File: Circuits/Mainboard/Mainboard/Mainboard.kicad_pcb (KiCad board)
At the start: 2 copper layers, 170 x 170 mm, 96 parts, among them IC1 LM74500QDDFRQ1, IC2 LM74500QDDFRQ1, IC3 2536030320001, IC4 SX1280IMLTRT, IC5 SKY66122-11, IC6 TPS563300DRLR, IC7 TPS563300DRLR, J1 XT60PW-M, J10 B5P-VH_LF__SN_, J11 B6B-PH-K-S, J12 B5P-VH_LF__SN_, J13 B6B-PH-K-S, J14 B5P-VH_LF__SN_, J15 SMA-J-P-H-RA-TH1, J16 B5P-VH_LF__SN_, J17 Conn_01x04_Pin, J2 XT60PW-M, J23 Conn_01x04_Pin, J24 Conn_01x06_Pin, J25 Conn_01x06_Pin, J26 Conn_01x04_Pin, J27 Conn_01x04_Pin, J3 Conn_01x06_Pin, J5 B6B-PH-K-S, J6 B5P-VH_LF__SN_, J7 B6B-PH-K-S, J8 Conn_01x06_Pin, J9 Conn_01x04_Pin, P1 66200621122, Q1 PSMN6R7-40MLDX, Q2 PSMN6R7-40MLDX, U1 NUCLEOH723ZG, U2 ADP121-AUJZ28R7

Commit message: Routing tracks
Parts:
- removed C14: 0.1uF, Capacitor_SMD:C_0805_2012Metric_Pad1.18x1.45mm_HandSolder
- removed C15, C17, C29, C31, C33: 100nF, Capacitor_SMD:C_0805_2012Metric_Pad1.18x1.45mm_HandSolder
- removed C16, C18, C30, C32, C34: 1nF, Capacitor_SMD:C_0805_2012Metric_Pad1.18x1.45mm_HandSolder
- removed C19: 1uF, Capacitor_SMD:C_0805_2012Metric_Pad1.18x1.45mm_HandSolder
- removed C20, C21: 10nF, Capacitor_SMD:C_0805_2012Metric_Pad1.18x1.45mm_HandSolder
- removed C35: 0p8, Capacitor_SMD:C_0805_2012Metric_Pad1.18x1.45mm_HandSolder
- removed C36: 1p5, Capacitor_SMD:C_0805_2012Metric_Pad1.18x1.45mm_HandSolder
- removed C37, C42: NA, Capacitor_SMD:C_0805_2012Metric_Pad1.18x1.45mm_HandSolder
- removed C38: 0p5, Capacitor_SMD:C_0805_2012Metric_Pad1.18x1.45mm_HandSolder
- removed C39: 100p, Capacitor_SMD:C_0805_2012Metric_Pad1.18x1.45mm_HandSolder
- removed C40: 47p, Capacitor_SMD:C_0805_2012Metric_Pad1.18x1.45mm_HandSolder
- removed C41: 0p6, Capacitor_SMD:C_0805_2012Metric_Pad1.18x1.45mm_HandSolder
- removed FB1, FB2: 120R, Resistor_SMD:R_0805_2012Metric_Pad1.20x1.40mm_HandSolder
- removed IC4: SX1280IMLTRT, SX1280IMLTRT:QFN50P400X400X100-25N-D
- removed IC5: SKY66122-11, SKY66122-11:QFN50P400X400X100-25N-D
- removed J15: SMA-J-P-H-RA-TH1, SMA-J-P-H-RA-TH1:SMAJPHRATH1
- removed R5: 3n, Resistor_SMD:R_0805_2012Metric_Pad1.20x1.40mm_HandSolder
- removed R6: 2n7, Resistor_SMD:R_0805_2012Metric_Pad1.20x1.40mm_HandSolder
- removed R7: 3n9, Resistor_SMD:R_0805_2012Metric_Pad1.20x1.40mm_HandSolder
- moved C24 156.3 mm to (198.9, 122.0), turned to -90 degrees
- moved C23 143.0 mm to (196.5, 139.8), turned to 180 degrees
- moved P1 138.6 mm to (254.9, 161.4), turned to 90 degrees
- moved C25 135.4 mm to (201.8, 122.0), turned to -90 degrees
- moved C26 130.6 mm to (195.3, 123.5)
- moved L2 126.7 mm to (194.3, 131.7)
- moved C13 126.5 mm to (175.8, 132.5)
- moved C10 126.1 mm to (190.1, 147.6)
- moved C7 126.0 mm to (190.7, 150.4)
- moved C12 123.0 mm to (167.2, 120.1), turned to -90 degrees
- moved C22 115.6 mm to (190.5, 140.6), turned to 180 degrees
- moved IC6 114.8 mm to (190.3, 144.4), turned to 90 degrees
- moved IC3 107.2 mm to (194.7, 120.2)
- moved R9 107.1 mm to (198.1, 144.7), turned to 90 degrees
- moved C44 104.1 mm to (169.6, 129.6)
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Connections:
- P1 pad 4: unconnected-(P1-Pad4) -> /LT3751_GPIO_INPUT
- P1 pad 5: unconnected-(P1-Pad5) -> /LT3751_GPIO_OUTPUT
- U1 pad CN8_7: 3.3V -> unconnected-(U1C-3V3_CN8-PadCN8_7)
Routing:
- net /VL6180_IO0: track 0.00 -> 157.9 mm, vias 0 -> 3
- net /M3_Encoder_A: track 0.00 -> 130.8 mm, vias 0 -> 1
- net /VL6180_SCL: track 0.00 -> 129.4 mm, vias 0 -> 3
- net /VL53L4CD_SDA: track 0.00 -> 112.8 mm, vias 0 -> 7
- net /ADPS-9960_INT: track 0.00 -> 110.9 mm, vias 0 -> 5
- net /ADPS-9960_SCL: track 0.00 -> 110.9 mm, vias 0 -> 3
- net /ADPS-9960_VL: track 0.00 -> 110.7 mm, vias 0 -> 2
- net /Rpi_RX: track 0.00 -> 109.0 mm, vias 0 -> 2
- net /M1_RX: track 0.00 -> 108.2 mm
- net /ADPS-9960_SDA: track 0.00 -> 106.4 mm
- net /M1_TX: track 0.00 -> 100.2 mm
- net /VL6180_IO1: track 0.00 -> 97.8 mm, vias 0 -> 5
- net /VL53L4CD_SCL: track 0.00 -> 97.8 mm, vias 0 -> 5
- net /M1_OUT1: track 96.5 -> 0.00 mm
- net /VL53L4CD_INT: track 0.00 -> 88.1 mm, vias 0 -> 4
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- added copper zone on F.Cu, net /24V_1
- added copper zone on F.Cu, net /24V_2
- added copper zone on F.Cu, net /M1_OUT1
- added copper zone on F.Cu, net /M1_OUT2
- added copper zone on F.Cu, net /M1_OUT3
- added copper zone on F.Cu, net /M3_OUT1
- added copper zone on B.Cu, net /M3_OUT2
- added copper zone on F.Cu, net /M3_OUT3

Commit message: Mainborad routing
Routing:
- net 5V: track 140.9 -> 515.6 mm, vias 1 -> 3
- net 3.3V: track 43.6 -> 223.5 mm, vias 0 -> 1
- net /VL6180_SDA: track 18.0 -> 190.4 mm, vias 1 -> 4
- net /M2_PWM: track 0.00 -> 122.1 mm, vias 0 -> 3
- net /VL53L4CD2_INT: track 0.00 -> 115.1 mm, vias 0 -> 2
- net /SEN0374_BL-IND: track 0.00 -> 108.2 mm, vias 0 -> 4
- net /VL53L4CD2_SHUT: track 0.00 -> 104.3 mm, vias 0 -> 5
- net /M4_TX: track 0.00 -> 102.2 mm, vias 0 -> 5
- net /M4_RX: track 0.00 -> 95.1 mm, vias 0 -> 1
- net /SEN0374_PS2: track 0.00 -> 93.7 mm, vias 0 -> 2
- net /M5_TX: track 0.00 -> 86.8 mm, vias 0 -> 1
- net /M5_RX: track 0.00 -> 78.8 mm, vias 0 -> 1
- net /M2_OUT1: track 0.00 -> 73.8 mm
- net /M4_Encoder_A: track 0.00 -> 73.0 mm, vias 0 -> 1
- net WSENS_SDA: track 0.00 -> 70.9 mm, vias 0 -> 2
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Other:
- board size 170 x 170 mm -> 170 x 135.9 mm

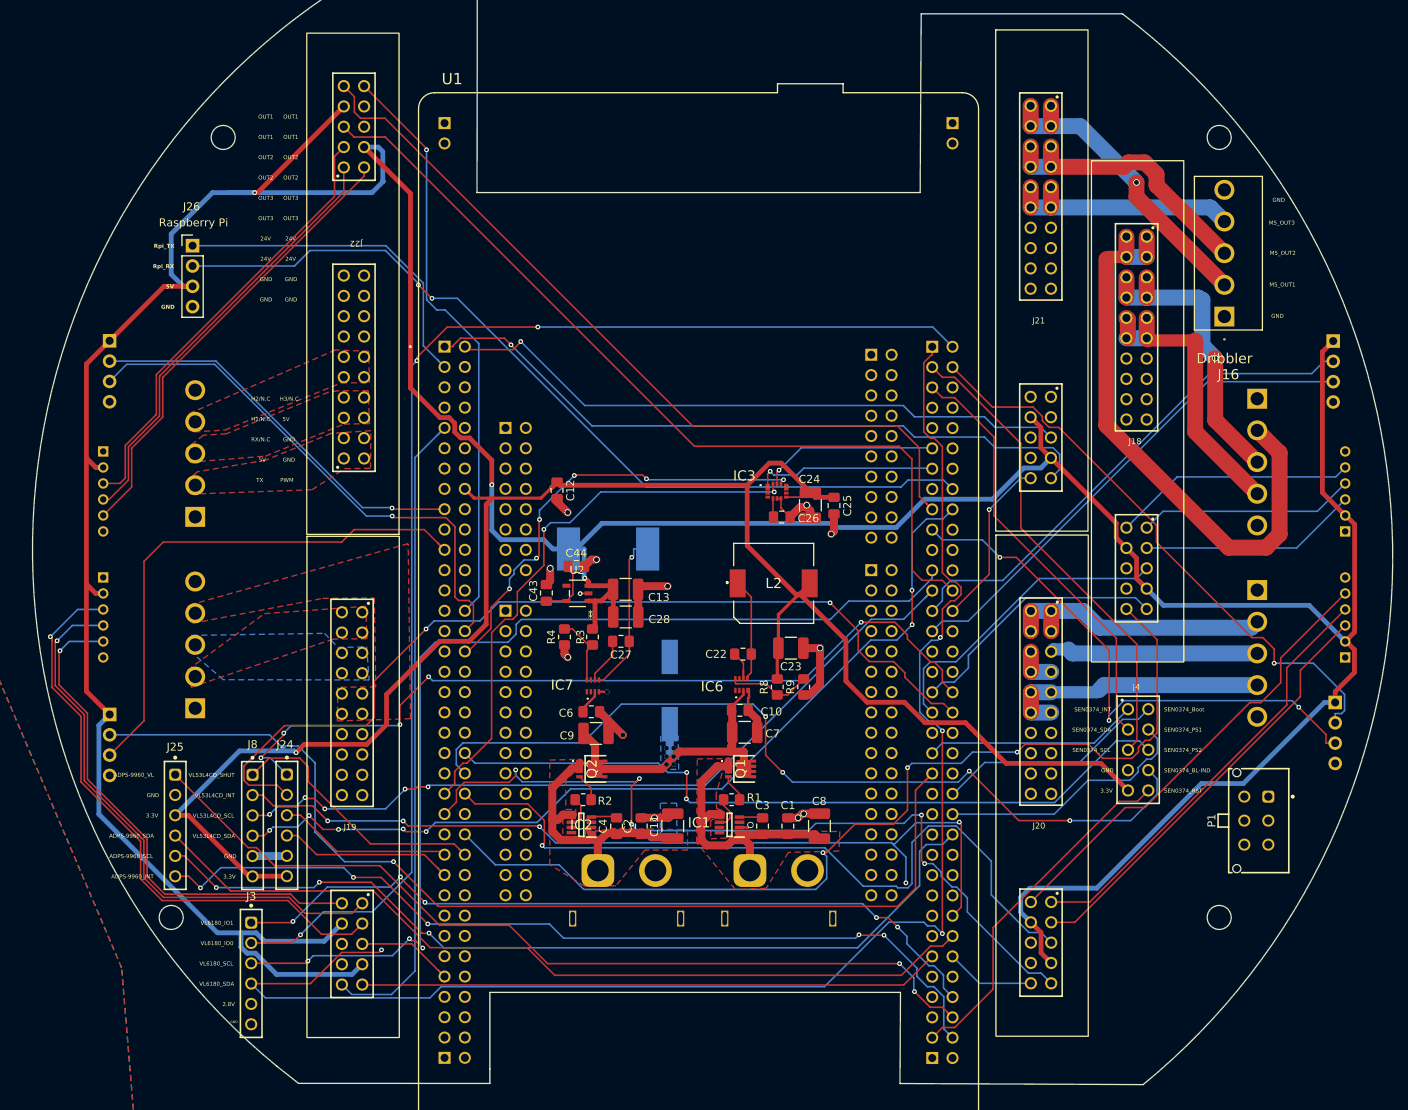
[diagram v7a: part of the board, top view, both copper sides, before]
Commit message: Encoder PCB done, with step file
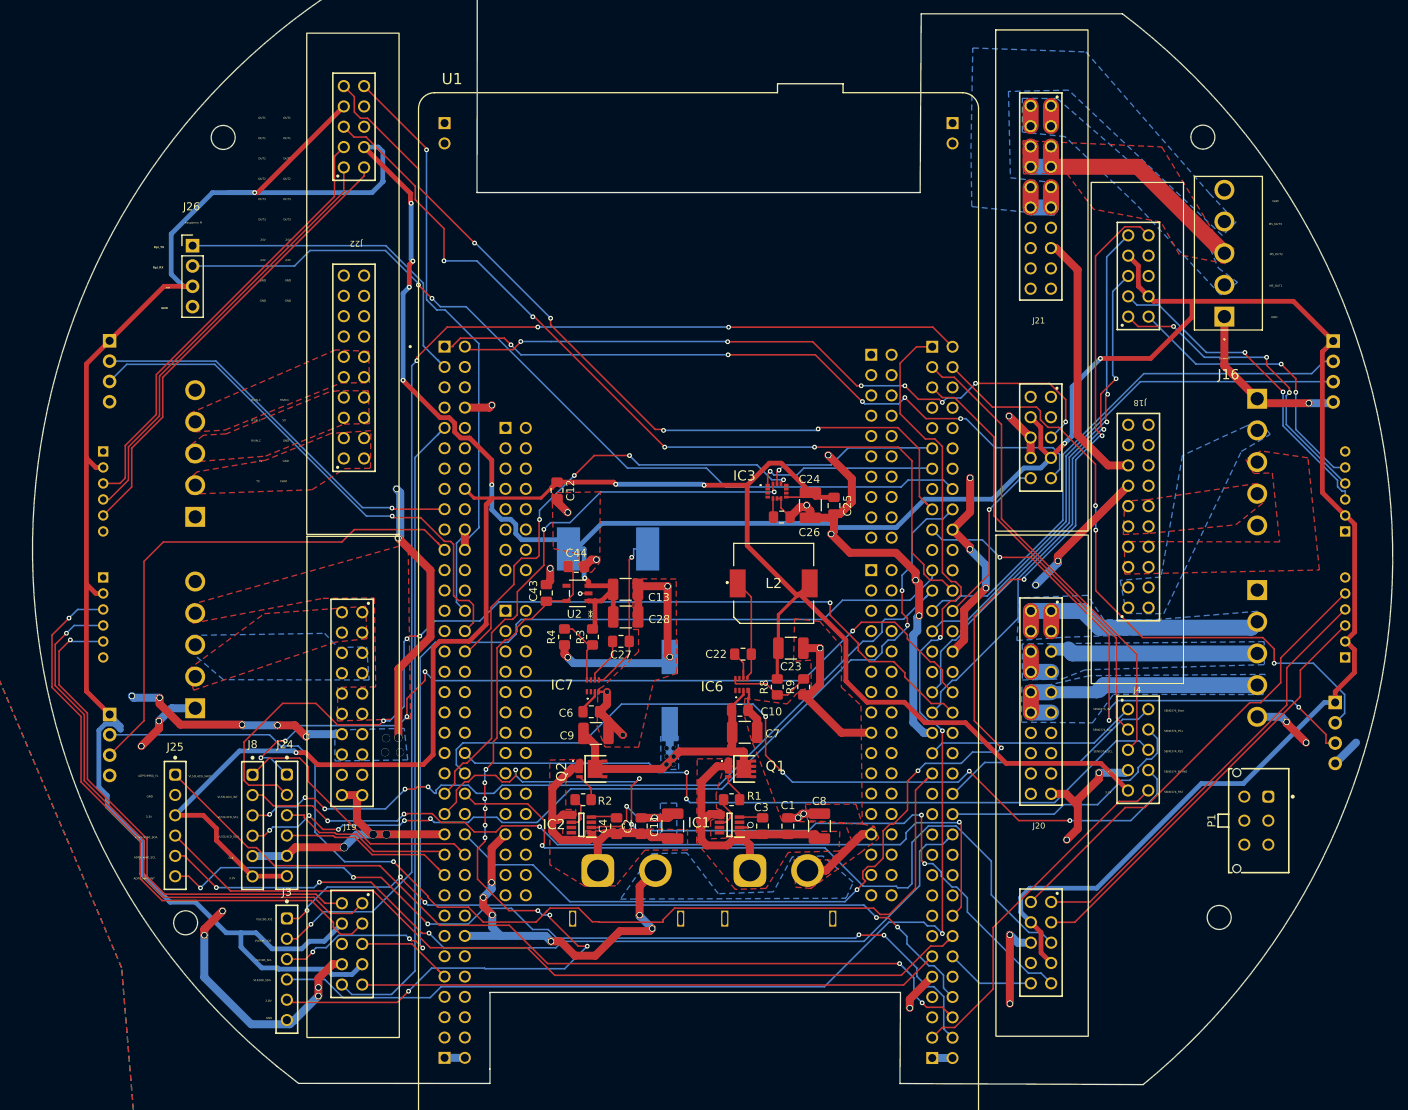
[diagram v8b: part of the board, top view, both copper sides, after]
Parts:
- moved J18 34.3 mm to (239.9, 128.7), turned to 180 degrees
- moved J3 4.49 mm to (133.5, 180.0)
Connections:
- P1 pad 1: unconnected-(P1-Pad1) -> GND
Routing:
- net GND: track 64.9 -> 401.2 mm, vias 15 -> 48
- net 24V: track 41.7 -> 155.5 mm, vias 6 -> 19
- net 2.8V: track 7.42 -> 104.6 mm, vias 0 -> 10
- net /M2_OUT1: track 73.8 -> 0.00 mm
- net /M2_PWM: track 122.1 -> 163.3 mm, vias 3 -> 5
- net /M2_OUT2: track 37.8 -> 0.00 mm, vias 1 -> 0
- net /M2_OUT3: track 36.4 -> 0.00 mm
- net /M2_TX: track 33.2 -> 67.9 mm, vias 0 -> 2
- net /M5_OUT1: track 38.6 -> 5.08 mm, vias 1 -> 0
- net /M2_RX: track 39.0 -> 65.8 mm, vias 0 -> 2
- net /M5_OUT3: track 30.0 -> 7.62 mm
- net 5V: track 515.6 -> 534.5 mm, vias 3 -> 9
- net /VL6180_SDA: track 190.4 -> 172.1 mm, vias 4 -> 3
- net /M2_H1: track 27.3 -> 41.3 mm, vias 0 -> 2
- net /M2_H2: track 27.1 -> 39.6 mm, vias 0 -> 3
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- added copper zone on B.Cu, net /M2_OUT1
- added copper zone on F.Cu, net /M2_OUT2
- added copper zone on F.Cu, net /M2_OUT3
- added copper zone on B.Cu, net /M4_OUT1
- added copper zone on B.Cu, net /M4_OUT2
- added copper zone on B.Cu, net /M4_OUT3
- added copper zone on B.Cu, net /M5_OUT1
- added copper zone on F.Cu, net /M5_OUT2
- added copper zone on B.Cu, net /M5_OUT3
- added copper zone on F.Cu, net GND
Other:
- outline, holes or cut-outs redrawn
